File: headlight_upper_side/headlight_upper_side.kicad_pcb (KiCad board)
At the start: 2 copper layers, 73 x 55 mm, 19 parts, among them J2 Conn_02x03_Odd_Even

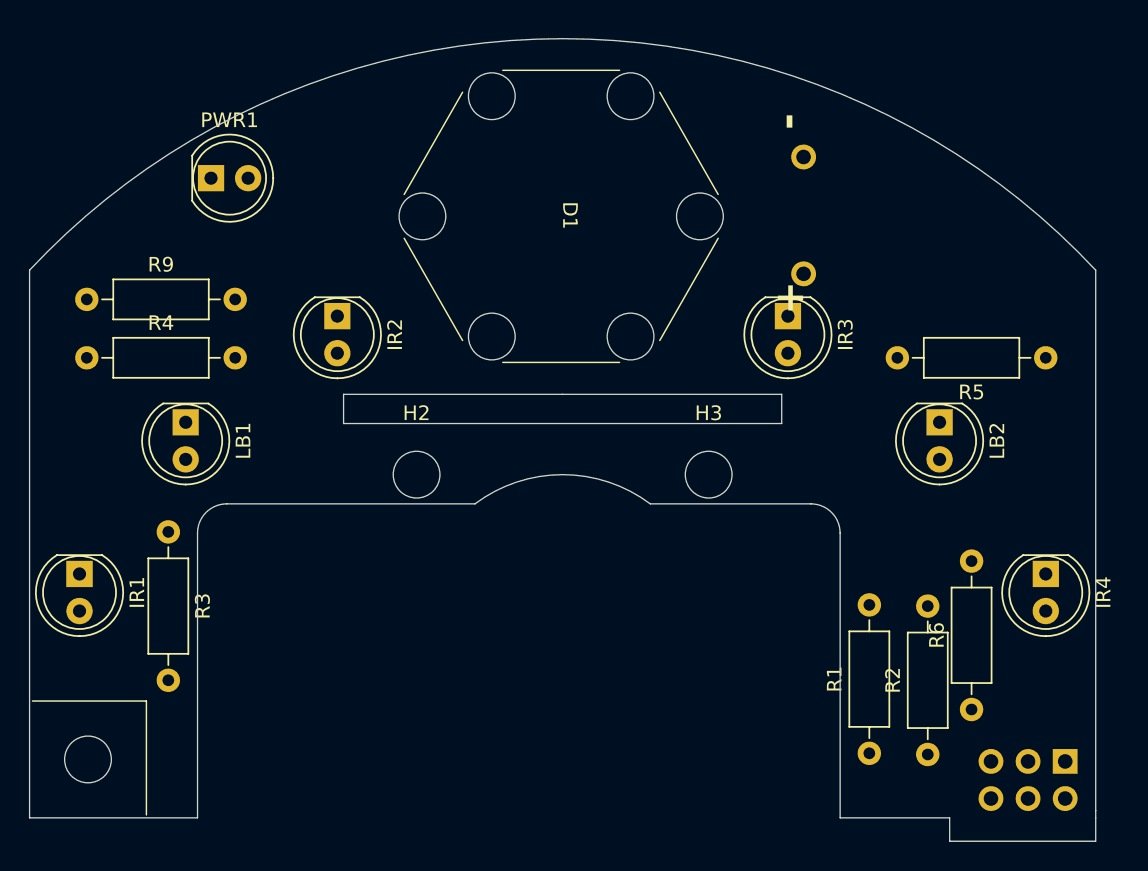
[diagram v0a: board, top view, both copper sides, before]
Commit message: 基板防水REV00発注完了
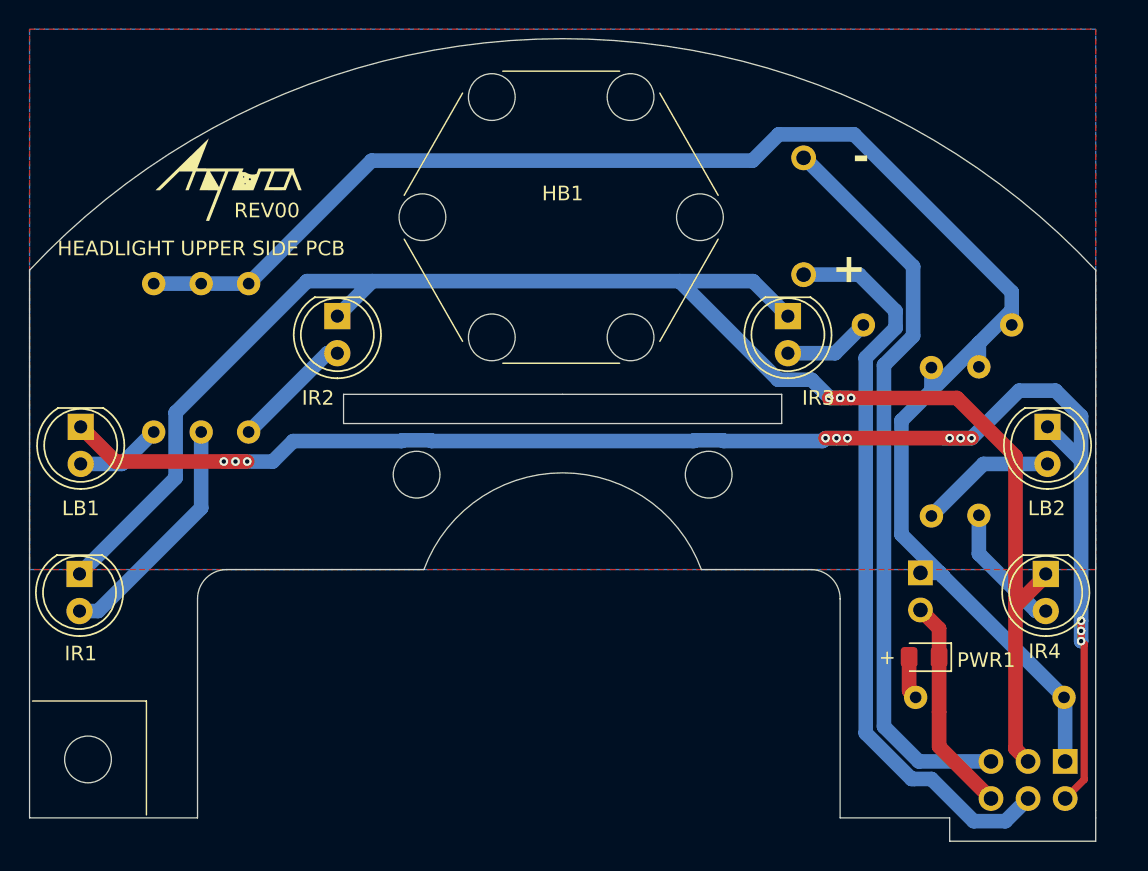
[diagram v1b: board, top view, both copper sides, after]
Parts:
- removed D1: high-power-led, high-power-led:power led
- added G***: LOGO, specific_library:aqua_rogo, F.Cu at (38.7, 32.2)
- added HB1: high-power-led, specific_library:power led, F.Cu at (61.7, 34.8)
- added M1: Fan, Connector_PinHeader_2.54mm:PinHeader_1x02_P2.54mm_Vertical, B.Cu at (86.2, 59.2)
- PWR1: value ~ -> BLUE; footprint LED_THT:LED_D5.0mm -> LED_SMD:LED_0805_2012Metric_Pad1.15x1.40mm_HandSolder
- R1, R2, R4, R5, R6: value 200 -> 180; moved to B.Cu
- R3: value 200 -> 100; moved to B.Cu
- R9: value 200 -> 750; moved to B.Cu
- moved R9 72.2 mm to (96.1, 67.7), turned to 180 degrees
- moved PWR1 58.8 mm to (86.5, 65.0), turned to 180 degrees
- moved R1 58.6 mm to (33.7, 39.4), turned to -90 degrees
- moved R2 26.5 mm to (87.0, 45.2), turned to -90 degrees
- moved R6 23.5 mm to (90.2, 45.1), turned to -90 degrees
- moved R3 17.1 mm to (37.0, 39.4)
- moved R4 12.2 mm to (40.2, 39.4), turned to -90 degrees
- moved LB2 7.40 mm to (94.9, 49.2)
- moved LB1 7.20 mm to (28.7, 49.2)
- moved R5 3.24 mm to (92.5, 42.2)
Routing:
- net IR: track 0.00 -> 117.4 mm, vias 0 -> 3
- net +5.1V: track 0.00 -> 113.2 mm
- net LB: track 0.00 -> 108.9 mm, vias 0 -> 12
- net HB_A: track 0.00 -> 51.4 mm
- net HB_K: track 0.00 -> 51.2 mm
- net Net-(IR1-A): track 0.00 -> 16.5 mm
- net GND: track 0.00 -> 14.9 mm
- net Net-(LB2-A): track 0.00 -> 9.43 mm
- net Net-(IR4-A): track 0.00 -> 8.84 mm
- net Net-(IR2-A): track 0.00 -> 8.31 mm
- net Net-(IR3-A): track 0.00 -> 5.97 mm
- net Net-(LB1-A): track 0.00 -> 5.91 mm
- net Net-(PWR1-A): track 0.00 -> 2.93 mm
- added copper zone on B.Cu, net (none)
- added copper zone on F.Cu, net (none)
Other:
- outline, holes or cut-outs redrawn
- board text added: "+"
- board text added: "HEADLIGHT UPPER SIDE PCB"
- board text added: "REV00"

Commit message: ヘッドライト基盤REV01作成
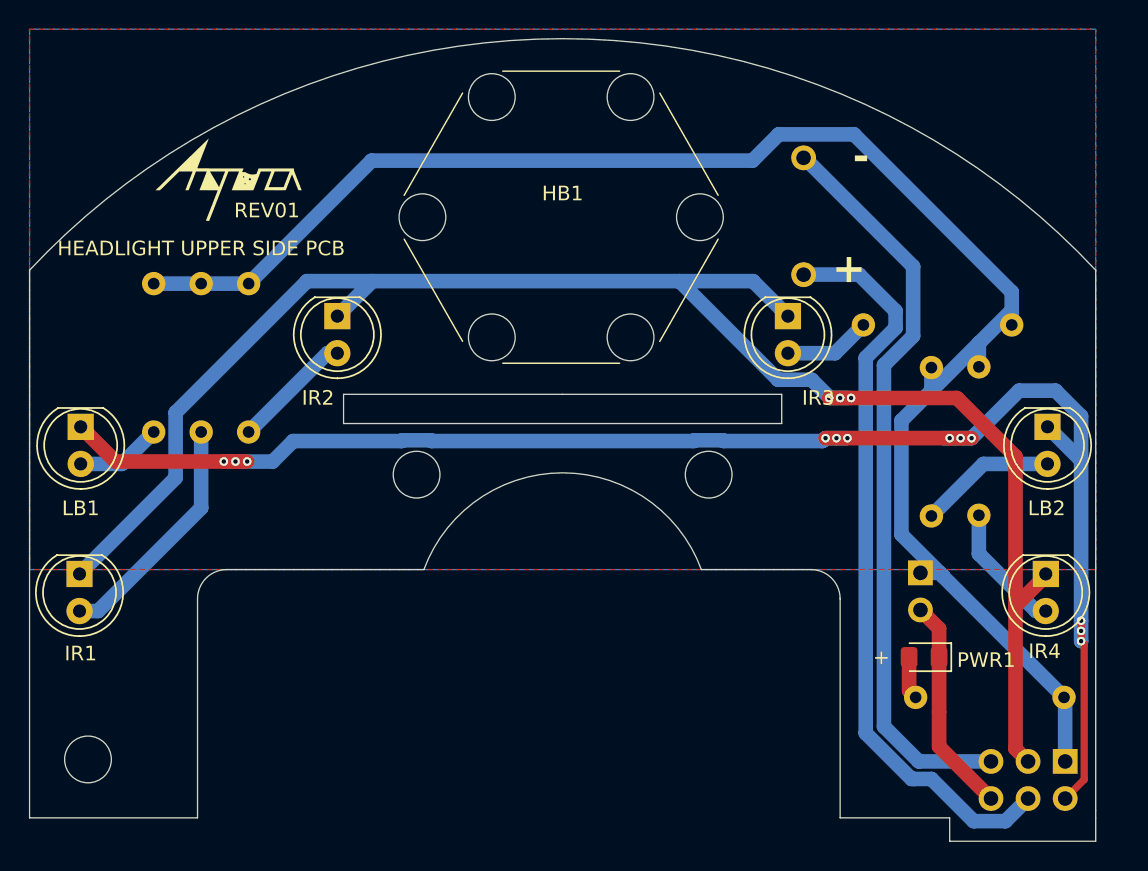
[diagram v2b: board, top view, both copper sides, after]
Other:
- board text added: "REV01"
- board text removed: "REV00"
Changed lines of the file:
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@@
 	(title_block
 		(title "headlight_upper_side")
-		(rev "00")
+		(rev "01")
 	)
 	(layers
@@
 		)
 		(property "Value" "180"
-			(at 5.08 -2.37 90)
-			(layer "B.Fab")
+			(at 5.08 0 90)
+			(layer "B.SilkS")
 			(effects
 				(font
@@
 		)
 		(property "Value" "750"
-			(at 5.08 -2.37 0)
-			(layer "B.Fab")
+			(at 5.08 0 0)
+			(layer "B.SilkS")
 			(effects
 				(font
@@
 		)
 		(property "Value" "180"
-			(at 5.08 -2.37 90)
-			(layer "B.Fab")
+			(at 5.08 0 90)
+			(layer "B.SilkS")
 			(effects
 				(font
@@
 		(property "Value" "Conn_02x03_Odd_Even"
 			(at -1.27 -7.85 90)
-			(layer "B.Fab")
+			(layer "B.SilkS")
+			(hide yes)
 			(effects
 				(font
@@
 		)
 		(property "Value" "180"
-			(at 5.08 -2.37 90)
-			(layer "B.Fab")
+			(at 5.08 0 90)
+			(layer "B.SilkS")
 			(effects
 				(font
@@
 		(property "Value" "Fan"
 			(at 0 -4.87 0)
-			(layer "B.Fab")
+			(layer "B.SilkS")
 			(effects
 				(font
@@
 		)
 		(property "Value" "180"
-			(at 5.08 -2.37 0)
-			(layer "B.Fab")
+			(at 5.08 0 0)
+			(layer "B.SilkS")
 			(effects
 				(font
@@
 		)
 		(property "Value" "180"
-			(at 5.08 -2.37 90)
-			(layer "B.Fab")
+			(at 5.03 0 90)
+			(layer "B.SilkS")
 			(effects
 				(font
@@
 		)
 		(property "Value" "100"
-			(at 5.08 -2.37 90)
-			(layer "B.Fab")
+			(at 5.08 0 90)
+			(layer "B.SilkS")
 			(effects
 				(font
@@
 	(gr_line
 		(start 33.249999 67.999999)
-		(end 25.449999 67.999999)
+		(end 33.249999 75.749999)
 		(stroke
 			(width 0.1)
 			(type default)
 		)
-		(layer "F.SilkS")
+		(layer "B.SilkS")
 	)
 	(gr_line
-		(start 33.249999 75.799999)
-		(end 33.249999 67.999999)
+		(start 33.249999 67.999999)
+		(end 25.499999 67.999999)
 		(stroke
 			(width 0.1)
 			(type default)
 		)
-		(layer "F.SilkS")
+		(layer "B.SilkS")
 	)
 	(gr_line
@@
 		)
 	)
-	(gr_text "REV00"
+	(gr_text "REV01"
 		(at 39.249999 34.999999 0)
 		(layer "F.SilkS")
@@
 	)
 	(gr_text "+"
-		(at 84.549999 65.599999 0)
+		(at 82.999999 65.599999 0)
 		(layer "F.SilkS")
 		(effects
@@
 				(thickness 0.1875)
 			)
-			(justify left bottom mirror)
+			(justify left bottom)
 		)
 	)
